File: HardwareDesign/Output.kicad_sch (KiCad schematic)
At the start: 18 parts, among them U401 74ACT157, U402 74ACT157, U403 74ACT574

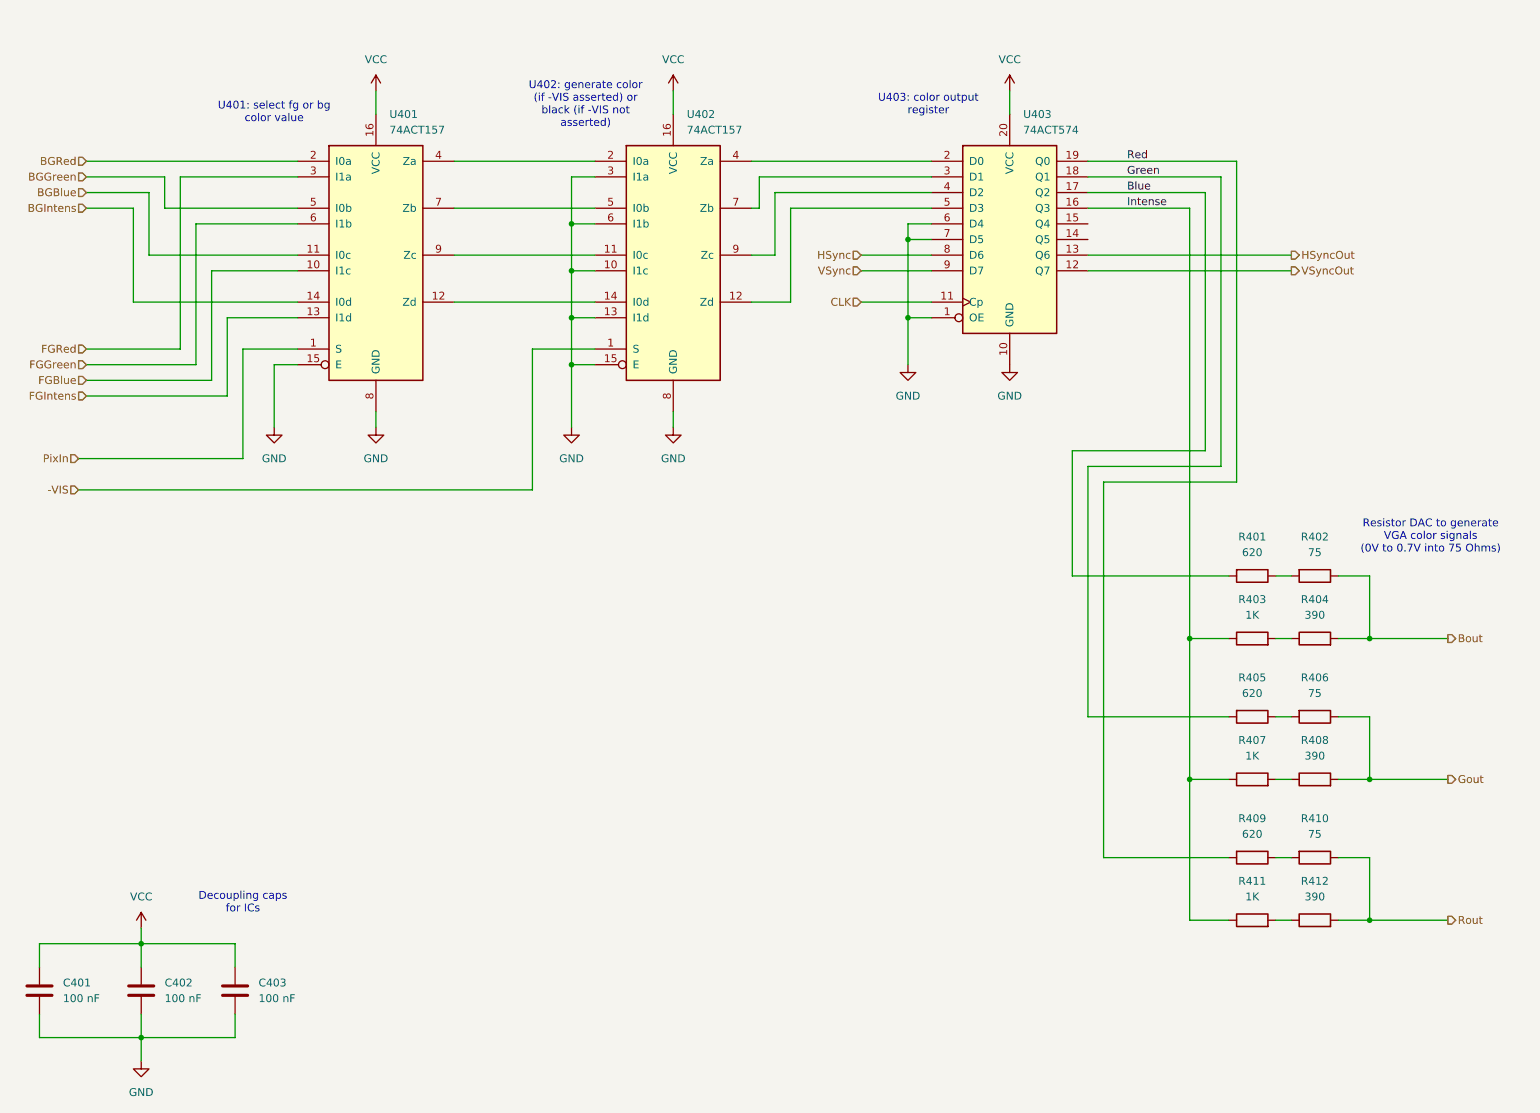
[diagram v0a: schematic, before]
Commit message: use enable input of U401 to blank invisible pixels
This eliminates the need for U402. This change has
been verified as working using the hard-wired
prototype.

Idea suggested by Episode 01 viewer RayBellis:
thank you, Ray!
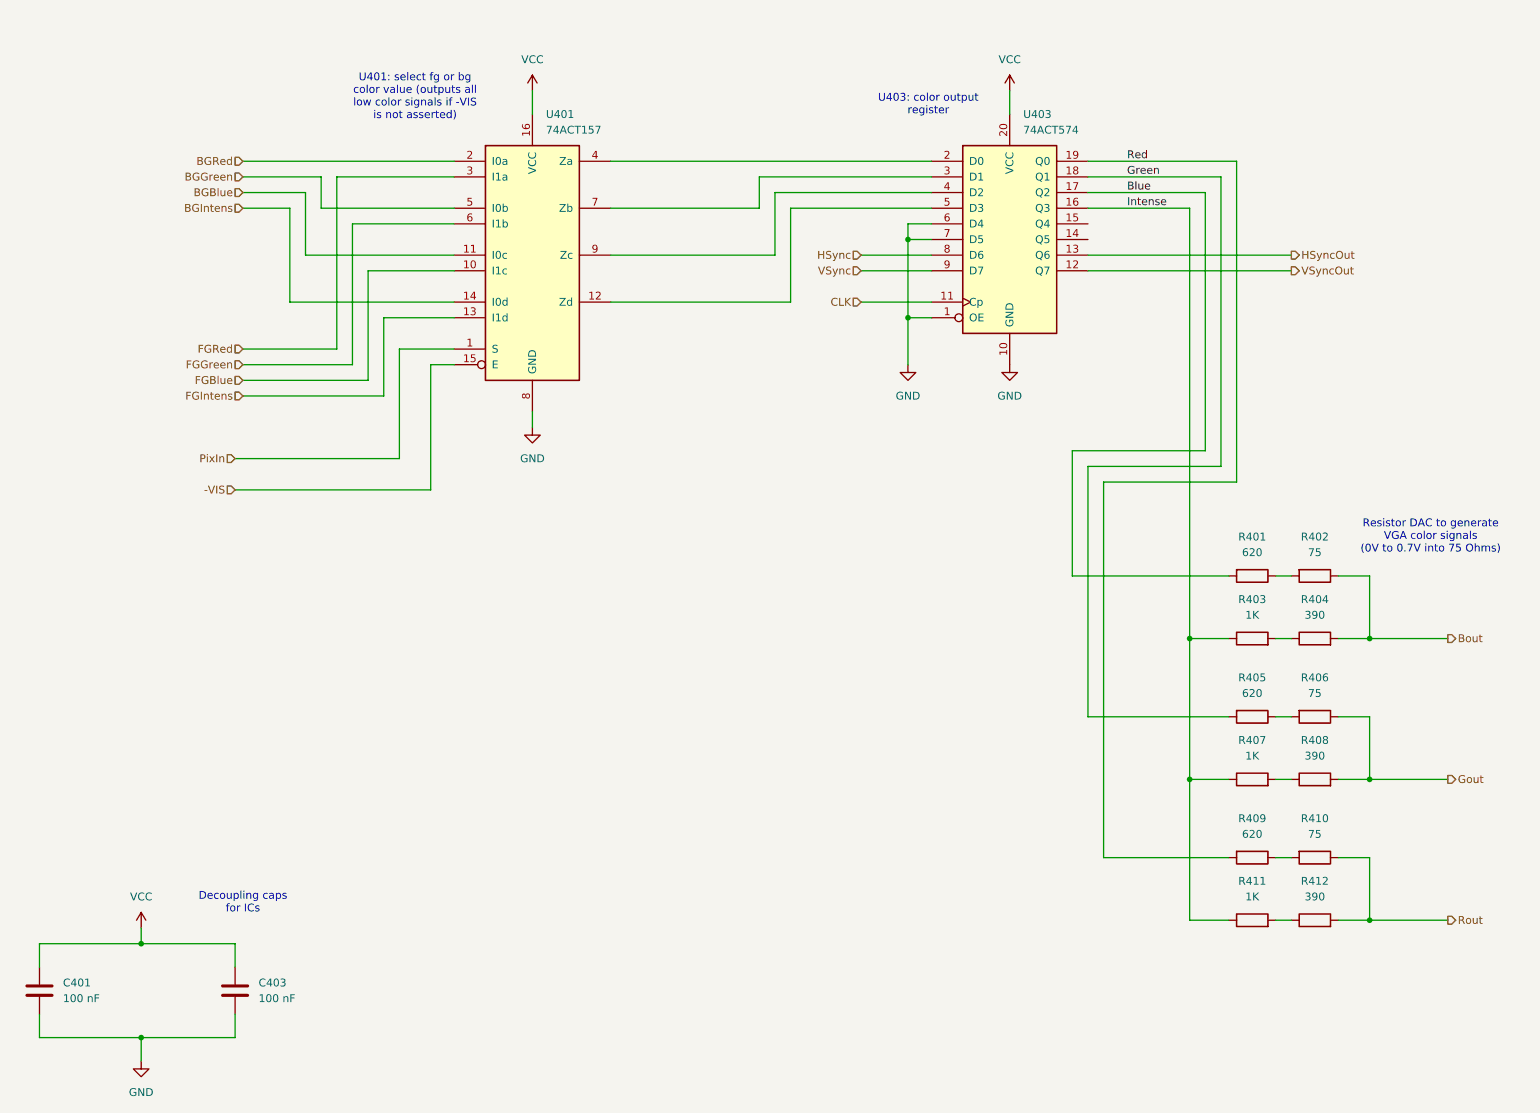
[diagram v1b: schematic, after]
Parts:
- removed C402: 100 nF, symbol Device:C
- removed U402: 74ACT157, symbol 74xx:74LS157
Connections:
- net -VIS: now also U401.15 (E)
- net GND: no longer U401.15 (E)
- net at U403.2 (D0): now also U401.4 (Za)
- net at U403.3 (D1): now also U401.7 (Zb)
- net at U403.4 (D2): now also U401.9 (Zc)
- net at U403.5 (D3): now also U401.12 (Zd)
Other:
- note added: "U401: select fg or bg color value (outputs all low color signals if -VIS is not asserted)"
- note removed: "U401: select fg or bg color value"
- note removed: "U402: generate color (if -VIS asserted) or black (if -VIS not asserted)"
- moved on the sheet: U401

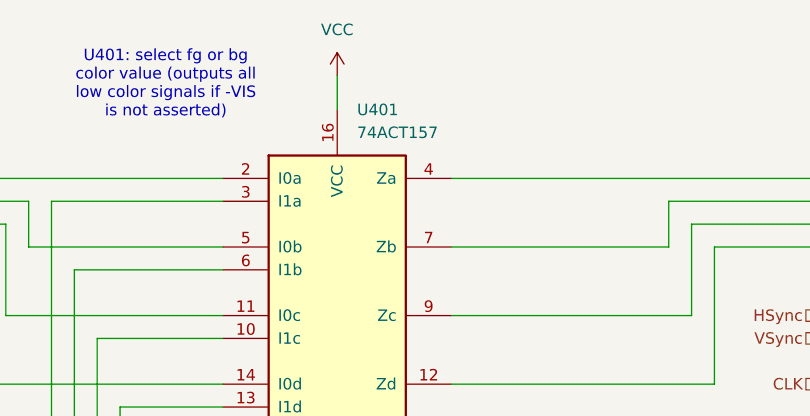
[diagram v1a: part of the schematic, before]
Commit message: use 74ALS157 instead of 74ACT157
There is very minor horizontal timing jitter when using the
74ACT157.

More generally, I think that aside from the video signal
output register, which needs to be CMOS in order to generate
correct VGA color signal voltage levels, all 74ACT parts
should be 74ALS parts.
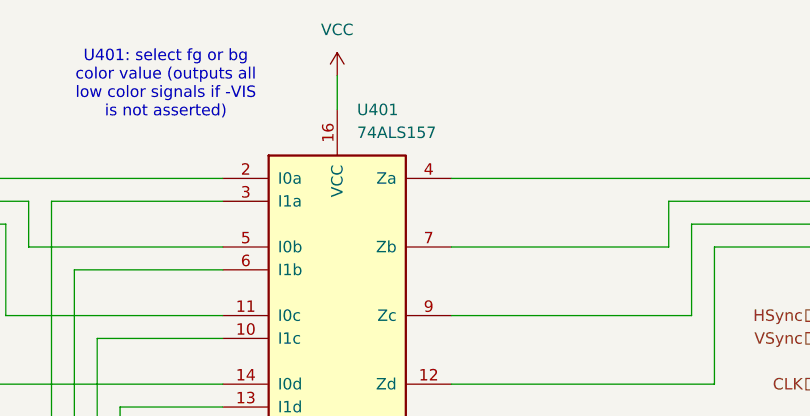
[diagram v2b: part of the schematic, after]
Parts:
- U401: value 74ACT157 -> 74ALS157
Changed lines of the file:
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@@
 			)
 		)
-		(property "Value" "74ACT157"
+		(property "Value" "74ALS157"
 			(at 108.8741 33.02 0)
 			(effects

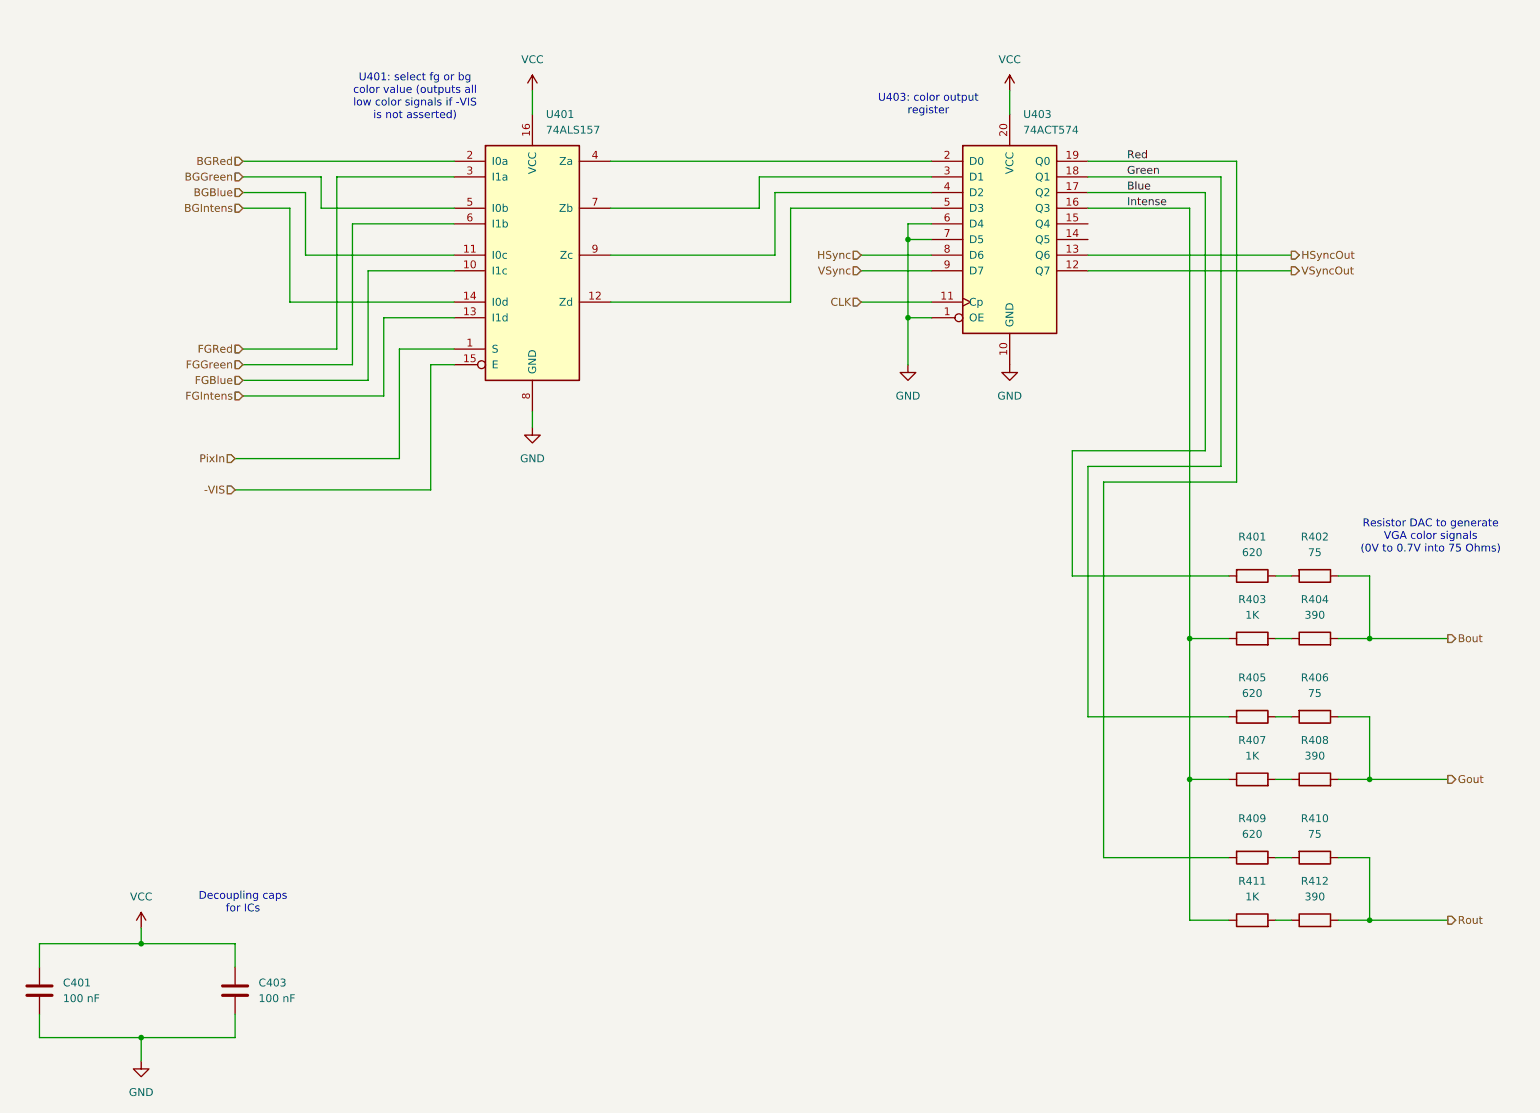
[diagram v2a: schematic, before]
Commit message: make HSync/VSync high 3V rather than 5V
Two of my VGA monitors are unhappy with 5V logic high
on HSync and VSync. Added a 2K/3K voltage divider for
each one. Monitors seem happy now.
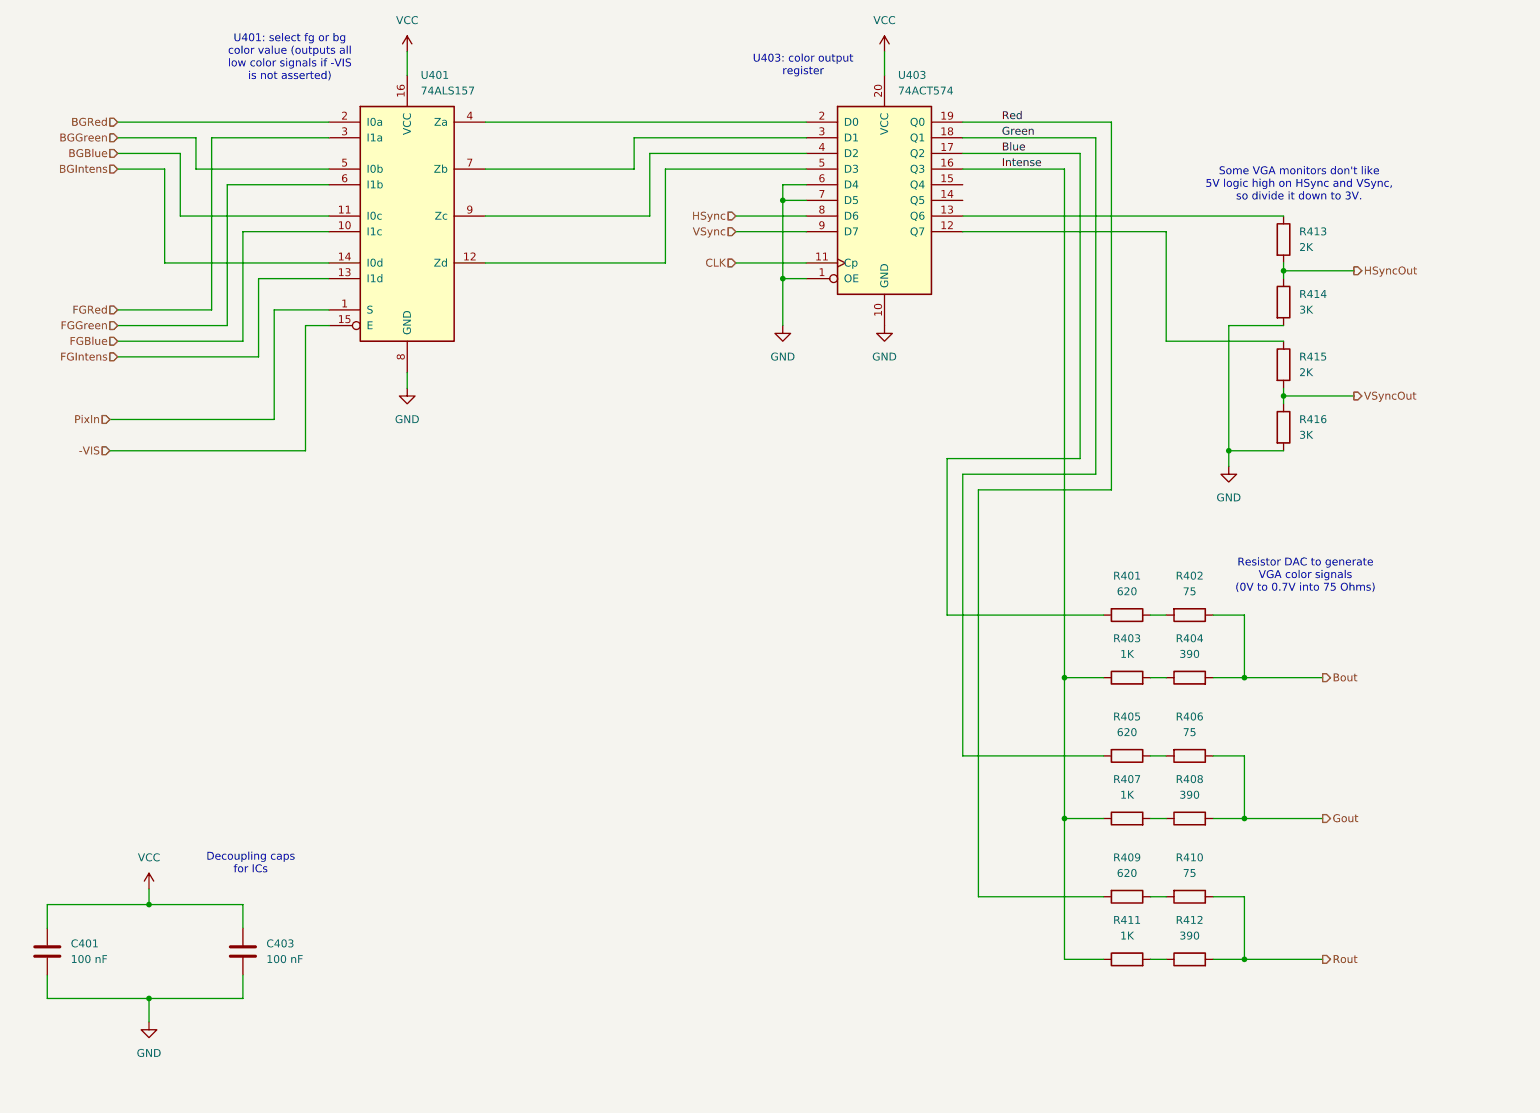
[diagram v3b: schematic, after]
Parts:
- added R413, R415: 2K, symbol Device:R
- added R414, R416: 3K, symbol Device:R
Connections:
- net GND: now also R414.2, R416.2
- net HSyncOut: now also R413.2, R414.1; no longer U403.13 (Q6)
- net VSyncOut: now also R415.2, R416.1; no longer U403.12 (Q7)
- new net: R415.1, U403.12 (Q7)
- new net: R413.1, U403.13 (Q6)
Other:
- note added: "Some VGA monitors don't like 5V logic high on HSync and VSync, so divide it down to 3V."
- moved on the sheet: C401, C403, R401, R402, R403, R404, R405, R406, R407, R408, R409, R410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
